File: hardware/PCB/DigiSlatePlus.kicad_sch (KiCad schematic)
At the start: 48 parts, among them J4 USB_B, Q1 2N2222, U1 ESP32-S3-WROOM-1, U10 SA15-11SRWA, U11 LM2596S-ADJ, U12 KA78M05_TO252, U13 LD1117S33TR_SOT223, U14 DW01A, U2 MAX7219, U3 SA15-11SRWA, U4 SA15-11SRWA, U5 SA15-11SRWA, U6 SA15-11SRWA, U7 SA15-11SRWA, U8 SA15-11SRWA, U9 SA15-11SRWA

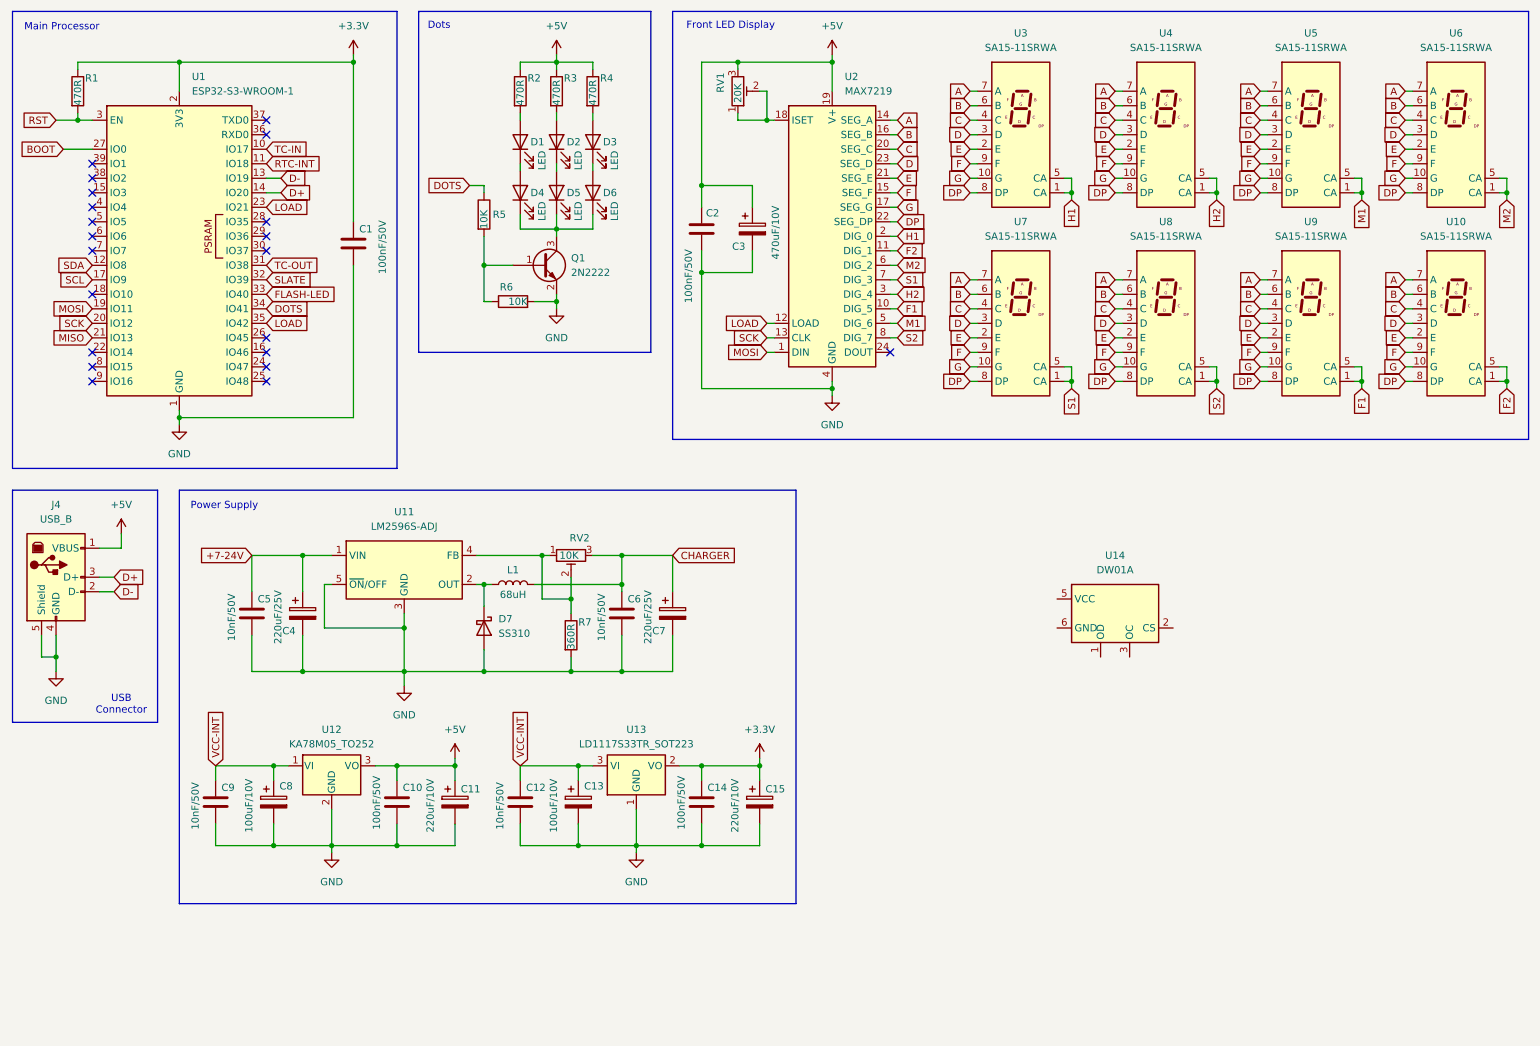
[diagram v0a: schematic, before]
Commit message: TP4056 library added
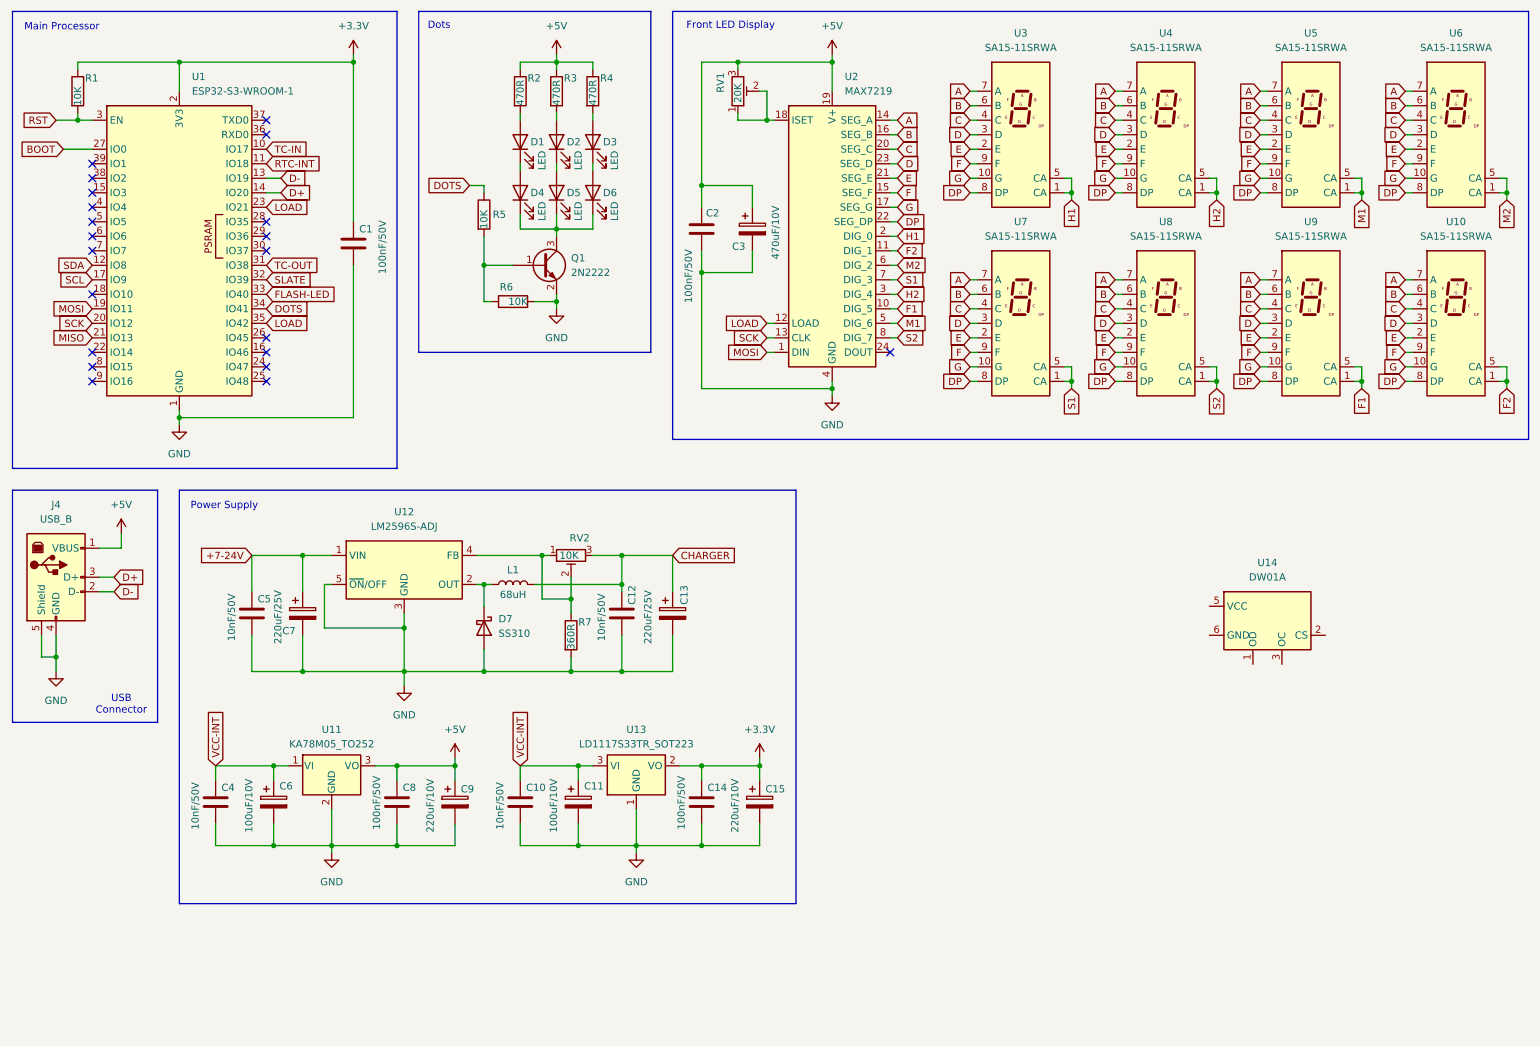
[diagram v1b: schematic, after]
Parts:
- R1: value 470R -> 10K
- renumbered C12 to C10, C13 to C11, C6 to C12, C7 to C13, C9 to C4, C8 to C6, C4 to C7, C10 to C8, C11 to C9, U12 to U11, U11 to U12
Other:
- moved on the sheet: U14
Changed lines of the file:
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@@
 		(on_board yes)
 		(dnp no)
-		(property "Reference" "C13"
+		(property "Reference" "C11"
 			(at 115.316 150.876 0)
 			(effects
@@
 			(project "DigiSlatePlus"
 				(path "/dcb9cf24-5afa-4bbe-8afa-a00529143e4d"
-					(reference "C13")
+					(reference "C11")
 					(unit 1)
 				)
@@
 		(dnp no)
 		(fields_autoplaced yes)
-		(property "Reference" "U12"
+		(property "Reference" "U11"
 			(at 71.12 140.97 0)
 			(effects
@@
 			(project ""
 				(path "/dcb9cf24-5afa-4bbe-8afa-a00529143e4d"
-					(reference "U12")
+					(reference "U11")
 					(unit 1)
 				)
@@
 	(symbol
 		(lib_id "Battery_Management:DW01A")
-		(at 208.28 120.65 0)
+		(at 234.95 121.92 0)
 		(unit 1)
 		(exclude_from_sim no)
@@
 		(fields_autoplaced yes)
 		(property "Reference" "U14"
-			(at 208.28 110.49 0)
+			(at 234.95 111.76 0)
 			(effects
 				(font
@@
 		)
 		(property "Value" "DW01A"
-			(at 208.28 113.03 0)
+			(at 234.95 114.3 0)
 			(effects
 				(font
@@
 		)
 		(property "Footprint" "Package_TO_SOT_SMD:SOT-23-6"
-			(at 208.28 120.65 0)
+			(at 234.95 121.92 0)
 			(effects
 				(font
@@
 		)
 		(property "Datasheet" "https://hmsemi.com/downfile/DW01A.PDF"
-			(at 208.28 120.65 0)
+			(at 234.95 121.92 0)
 			(effects
 				(font
@@
 		)
 		(property "Description" "Overcharge, overcurrent and overdischarge protection IC for single cell lithium-ion/polymer battery"
-			(at 208.534 119.126 0)
+			(at 235.204 120.396 0)
 			(effects
 				(font
@@
 		(on_board yes)
 		(dnp no)
-		(property "Reference" "C4"
+		(property "Reference" "C7"
 			(at 62.484 123.698 0)
 			(effects
@@
 			(project "DigiSlatePlus"
 				(path "/dcb9cf24-5afa-4bbe-8afa-a00529143e4d"
-					(reference "C4")
+					(reference "C7")
 					(unit 1)
 				)
@@
 		(on_board yes)
 		(dnp no)
-		(property "Reference" "C6"
-			(at 122.936 118.11 0)
+		(property "Reference" "C12"
+			(at 123.698 119.126 90)
 			(effects
 				(font
@@
 			(project "DigiSlatePlus"
 				(path "/dcb9cf24-5afa-4bbe-8afa-a00529143e4d"
-					(reference "C6")
+					(reference "C12")
 					(unit 1)
 				)
@@
 		(on_board yes)
 		(dnp no)
-		(property "Reference" "C12"
+		(property "Reference" "C10"
 			(at 105.156 151.13 0)
 			(effects
@@
 			(project "DigiSlatePlus"
 				(path "/dcb9cf24-5afa-4bbe-8afa-a00529143e4d"
-					(reference "C12")
+					(reference "C10")
 					(unit 1)
 				)
@@
 		(on_board yes)
 		(dnp no)
-		(property "Reference" "C10"
+		(property "Reference" "C8"
 			(at 83.566 151.13 0)
 			(effects
@@
 			(project "DigiSlatePlus"
 				(path "/dcb9cf24-5afa-4bbe-8afa-a00529143e4d"
-					(reference "C10")
+					(reference "C8")
 					(unit 1)
 				)
@@
 		(on_board yes)
 		(dnp no)
-		(property "Reference" "C8"
+		(property "Reference" "C6"
 			(at 61.976 150.876 0)
 			(effects
@@
 			(project "DigiSlatePlus"
 				(path "/dcb9cf24-5afa-4bbe-8afa-a00529143e4d"
-					(reference "C8")
+					(reference "C6")
 					(unit 1)
 				)
@@
 		(on_board yes)
 		(dnp no)
-		(property "Reference" "C9"
+		(property "Reference" "C4"
 			(at 51.816 151.13 0)
 			(effects
@@
 			(project "DigiSlatePlus"
 				(path "/dcb9cf24-5afa-4bbe-8afa-a00529143e4d"
-					(reference "C9")
+					(reference "C4")
 					(unit 1)
 				)
@@
 		(dnp no)
 		(fields_autoplaced yes)
-		(property "Reference" "U11"
+		(property "Reference" "U12"
 			(at 83.82 102.87 0)
 			(effects
@@
 			(project ""
 				(path "/dcb9cf24-5afa-4bbe-8afa-a00529143e4d"
-					(reference "U11")
+					(reference "U12")
 					(unit 1)
 				)
@@
 			)
 		)
-		(property "Value" "470R"
+		(property "Value" "10K"
 			(at 26.67 31.75 90)
 			(effects
@@
 		(on_board yes)
 		(dnp no)
-		(property "Reference" "C11"
+		(property "Reference" "C9"
 			(at 93.726 151.384 0)
 			(effects
@@
 			(project "DigiSlatePlus"
 				(path "/dcb9cf24-5afa-4bbe-8afa-a00529143e4d"
-					(reference "C11")
+					(reference "C9")
 					(unit 1)
 				)
@@
 		(on_board yes)
 		(dnp no)
-		(property "Reference" "C7"
-			(at 127.254 123.698 0)
+		(property "Reference" "C13"
+			(at 132.842 119.126 90)
 			(effects
 				(font
@@
 			(project "DigiSlatePlus"
 				(path "/dcb9cf24-5afa-4bbe-8afa-a00529143e4d"
-					(reference "C7")
+					(reference "C13")
 					(unit 1)
 				)

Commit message: Schematic updated
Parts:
- removed C10, C12, C4, C5: 10nF/50V, Capacitor_SMD:C_1206_3216Metric_Pad1.33x1.80mm_HandSolder, symbol Device:C
- removed C11, C6: 100uF/10V, Capacitor_Tantalum_SMD:CP_EIA-7343-31_Kemet-D_Pad2.25x2.55mm_HandSolder, symbol Device:C_Polarized
- removed C13, C7: 220uF/25V, Capacitor_Tantalum_SMD:CP_EIA-7343-31_Kemet-D_Pad2.25x2.55mm_HandSolder, symbol Device:C_Polarized
- removed C14, C8: 100nF/50V, Capacitor_SMD:C_1206_3216Metric_Pad1.33x1.80mm_HandSolder, symbol Device:C
- removed C15, C9: 220uF/10V, Capacitor_Tantalum_SMD:CP_EIA-7343-31_Kemet-D_Pad2.25x2.55mm_HandSolder, symbol Device:C_Polarized
- removed D7: SS310, Diode_SMD:D_SMA, symbol Diode:SS310
- removed L1: 68uH, Inductor_SMD:L_7.3x7.3_H3.5, symbol Device:L
- removed R7: 360R, Resistor_SMD:R_1206_3216Metric, symbol Device:R
- removed RV2: 10K, Potentiometer_THT:Potentiometer_Bourns_3296W_Vertical, symbol Device:R_Potentiometer_Trim
- removed U11: KA78M05_TO252, Package_TO_SOT_SMD:TO-252-2, symbol Regulator_Linear:KA78M05_TO252
- removed U12: LM2596S-ADJ, Package_TO_SOT_SMD:TO-263-5_TabPin6, symbol Regulator_Switching:LM2596S-ADJ
- removed U13: LD1117S33TR_SOT223, Package_TO_SOT_SMD:SOT-223-3_TabPin2, symbol Regulator_Linear:LD1117S33TR_SOT223
- removed U14: DW01A, Package_TO_SOT_SMD:SOT-23-6, symbol Battery_Management:DW01A
- added BT1: Battery_Cell, Battery:BatteryHolder_ComfortableElectronic_CH273-2450_1x2450, symbol Device:Battery_Cell
- added C17, C18: 100nF/50V, Capacitor_SMD:C_1206_3216Metric_Pad1.33x1.80mm_HandSolder, symbol Device:C
- added DS1: WC1602A, Display:WC1602A, symbol 7-Segment:WC1602A
- added R13, R14: 4K7, Resistor_SMD:R_1206_3216Metric, symbol Device:R
- added R15: 470R, Resistor_SMD:R_1206_3216Metric, symbol Device:R
- added R16, R17, R18: 10K, Resistor_SMD:R_1206_3216Metric, symbol Device:R
- added RV3: 20K, Potentiometer_SMD:Potentiometer_Vishay_TS53YL_Vertical, symbol Device:R_Potentiometer_Trim
- added SW1: RotaryEncoder-SW, Rotary_Encoder:RotaryEncoder_Bourns_Horizontal_PEC12R-2x17F-Sxxxx, symbol Device:RotaryEncoder_Switch_MP
- added U16: DS3231M, Package_SO:SOIC-16W_7.5x10.3mm_P1.27mm, symbol Timer_RTC:DS3231M
- J4: footprint (none) -> Connector_USB:USB_B_Lumberg_2411_02_Horizontal
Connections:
- net +3.3V: now also C17.1, R13.1, R14.1, R15.1, R16.1, R17.1, R18.1, U16.2 (VCC)
- net +5V: now also DS1.15 (LED(+)), DS1.2 (VDD), RV3.1, RV3.2
- net GND: now also BT1.2 (-), C17.2, C18.2, DS1.1 (VSS), DS1.16 (LED(-)), DS1.5 (R/W), SW1.C, SW1.MP, SW1.S2, U16.10 (GND), U16.11 (GND), U16.12 (GND), U16.13 (GND), U16.5 (GND), U16.6 (GND), U16.7 (GND), U16.8 (GND), U16.9 (GND)
- net RTC-INT: now also R15.2, U16.3 (~{INT}/SQW)
- net SCL: now also R13.2, U16.16 (SCL)
- net SDA: now also R14.2, U16.15 (SDA)
- net D6: now reaches U1.15 (IO3)
- net D6: now also DS1.13 (D6)
- net ROT-CLK: now reaches U1.16 (IO46)
- net ROT-CLK: now also R17.2, SW1.A
- net ROT-DT: now reaches U1.24 (IO47)
- net ROT-DT: now also R16.2, SW1.B
- net ROT-SW: now reaches U1.25 (IO48)
- net ROT-SW: now also R18.2, SW1.S1
- net LOAD-SC: now reaches U1.26 (IO45)
- net D5: now reaches U1.38 (IO2)
- net D5: now also DS1.12 (D5)
- net D4: now reaches U1.39 (IO1)
- net D4: now also DS1.11 (D4)
- net D7: now reaches U1.4 (IO4)
- net D7: now also DS1.14 (D7)
- net CE: now reaches U1.5 (IO5)
- net CE: now also DS1.6 (E)
- net RS: now reaches U1.6 (IO6)
- net RS: now also DS1.4 (RS)
- new net: DS1.3 (VO), RV3.3
- new net: BT1.1 (+), C18.1, U16.14 (VBAT)
- no-connect marks 21 -> 17
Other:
- added sheet Power (DigiSlatePlus-Power.kicad_sch)
- added sheet Scene Display (Scene_Display.kicad_sch)
- note added: "LC-Display"
- note added: "Real-Time-Clock"
- note added: "Rotary Encoder"
- note removed: "Power Supply"

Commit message: change page structure
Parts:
- removed C2: 100nF/50V, Capacitor_SMD:C_1206_3216Metric_Pad1.33x1.80mm_HandSolder, symbol Device:C
- removed C3: 470uF/10V, Capacitor_Tantalum_SMD:CP_EIA-7343-31_Kemet-D_Pad2.25x2.55mm_HandSolder, symbol Device:C_Polarized
- removed D1, D2, D3, D4, D5, D6: LED, LED_THT:LED_D3.0mm_FlatTop, symbol Device:LED
- removed Q1: 2N2222, Package_TO_SOT_SMD:SOT-23, symbol Transistor_BJT:MMBT2222A
- removed R2, R3, R4: 470R, Resistor_SMD:R_1206_3216Metric, symbol Device:R
- removed R5, R6: 10K, Resistor_SMD:R_1206_3216Metric, symbol Device:R
- removed RV3: 20K, Potentiometer_SMD:Potentiometer_Vishay_TS53YL_Vertical, symbol Device:R_Potentiometer_Trim
- removed U10, U3, U4, U5, U6, U7, U8, U9: SA15-11SRWA, 7-segment-led:FYS-12011A, symbol Display_Character:SA15-11SRWA
- removed U2: MAX7219, Package_SO:SOIC-24W_7.5x15.4mm_P1.27mm, symbol Driver_LED:MAX7219
- added J1: Serial, Connector_JST:JST_XH_B5B-XH-AM_1x05_P2.50mm_Vertical, symbol Connector_Generic:Conn_01x05
- renumbered C17 to C2, C18 to C3, J4 to J2, R16 to R2, R17 to R3, R18 to R4, R13 to R5, R14 to R6, R15 to R7, U16 to U2
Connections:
- net +3.3V: now also J1.4 (Pin_4)
- net +5V: now also RV1.1, RV1.2; no longer RV1.3
- net GND: now also J1.5 (Pin_5)
- net RST: now also J1.1 (Pin_1)
- net SW1: now reaches U1.18 (IO10)
- net SW2: now reaches U1.22 (IO14)
- net RX0: now reaches U1.36 (RXD0)
- net RX0: now also J1.2 (Pin_2)
- net TX0: now reaches U1.37 (TXD0)
- net TX0: now also J1.3 (Pin_3)
- net CLAP-LED: now reaches U1.7 (IO7)
- net SW3: now reaches U1.8 (IO15)
- net SW4: now reaches U1.9 (IO16)
- net at DS1.3 (VO): now also RV1.3
- no-connect marks 17 -> 10
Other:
- removed sheet Scene Display
- added sheet Timecode Display (tc_display.kicad_sch)
- note added: "Serial"
- note added: "USB"
- note removed: "Dots"
- note removed: "Front LED Display"
- note removed: "USB Connector"
- moved on the sheet: BT1, C2, C3, J2, R2, R3, R4, R5, R6, R7, SW1, U2
